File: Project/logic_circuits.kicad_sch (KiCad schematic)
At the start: 9 parts, among them SW1 Conn_01x02, U1 74LS04, U2 74LS93, U3 74LS08, U4 74LS32

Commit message: routing complete
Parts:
- removed unit 3 of U1
- removed unit 5 of U1
- removed unit 4 of U1
- added C8: 1uF, Capacitor_THT:CP_Radial_D5.0mm_P2.50mm, symbol Device:C
- added J1: Conn_01x04, Connector_PinHeader_2.54mm:PinHeader_1x04_P2.54mm_Vertical, symbol Connector_Generic:Conn_01x04
- added J2: Conn_02x07_Odd_Even, Connector_PinHeader_2.54mm:PinHeader_2x07_P2.54mm_Vertical, symbol Connector_Generic:Conn_02x07_Odd_Even
- added R3, R4, R5, R6, R7, R8, R9: 560, Resistor_THT:R_Axial_DIN0207_L6.3mm_D2.5mm_P7.62mm_Horizontal, symbol Device:R
- added unit 5 of U2
- added unit 3 of U2
- added unit 4 of U2
- renumbered C1 to C6, C2 to C7, U1 to U2, U2 to U5
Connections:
- net GND: now also U3.1, U3.2, C8.2, J1.4 (Pin_4), J2.10 (Pin_10), J2.12 (Pin_12), J2.14 (Pin_14), J2.2 (Pin_2), J2.4 (Pin_4), J2.6 (Pin_6), J2.8 (Pin_8); no longer U3.10, U3.9
- net Q0: now also U3.10, U2.9; no longer U3.1
- net Q1: now also U2.11
- net Q2: now also U3.9, U2.5; no longer U3.2
- net VCC: now also C8.1
- net a: now also R3.1, R8.1
- net b: now also U3.8, R4.1, R7.1; no longer U3.3
- net c: now also R5.1, R6.1
- net g: now also R9.1
- new net LED1: J2.1 (Pin_1), R3.2
- new net LED2: J2.3 (Pin_3), R4.2
- new net LED3: J2.5 (Pin_5), R5.2
- new net LED4: J2.7 (Pin_7), R6.2
- new net LED5: J2.9 (Pin_9), R7.2
- new net LED6: J2.11 (Pin_11), R8.2
- new net LED7: J2.13 (Pin_13), R9.2
- new net ~{Q0}: J1.1 (Pin_1), U2.8
- new net ~{Q1}: J1.2 (Pin_2), U2.10
- new net ~{Q2}: J1.3 (Pin_3), U2.6
- no-connect marks 7 -> 4
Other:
- note added: "Debug Output"
- note added: "Digital Dice Leds Layout"
- note added: "a"
- note added: "b"
- note added: "c"
- note added: "d"
- note added: "e"
- note added: "f"
- note added: "g"
- company: (none) -> Marcos Yonamine
- title: (none) -> Digital Dice
- moved on the sheet: C6, C7, R1, R2, SW1, U2A, U2B, U2F, U3B, U3D, U4A, U4B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

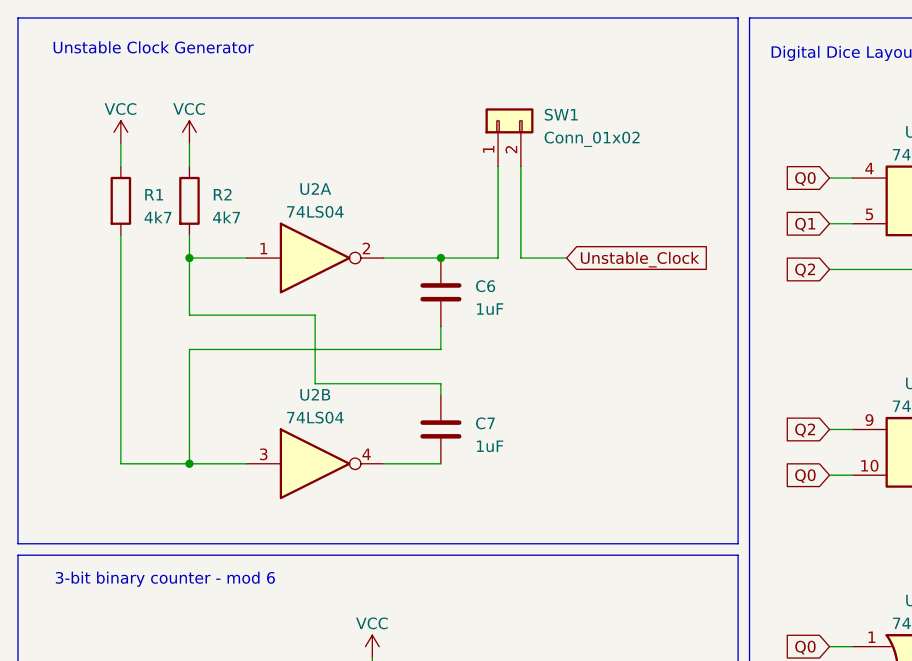
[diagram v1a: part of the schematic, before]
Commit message: fix #3
Latch was not unstable. Changed R1 and R2 to pulldown
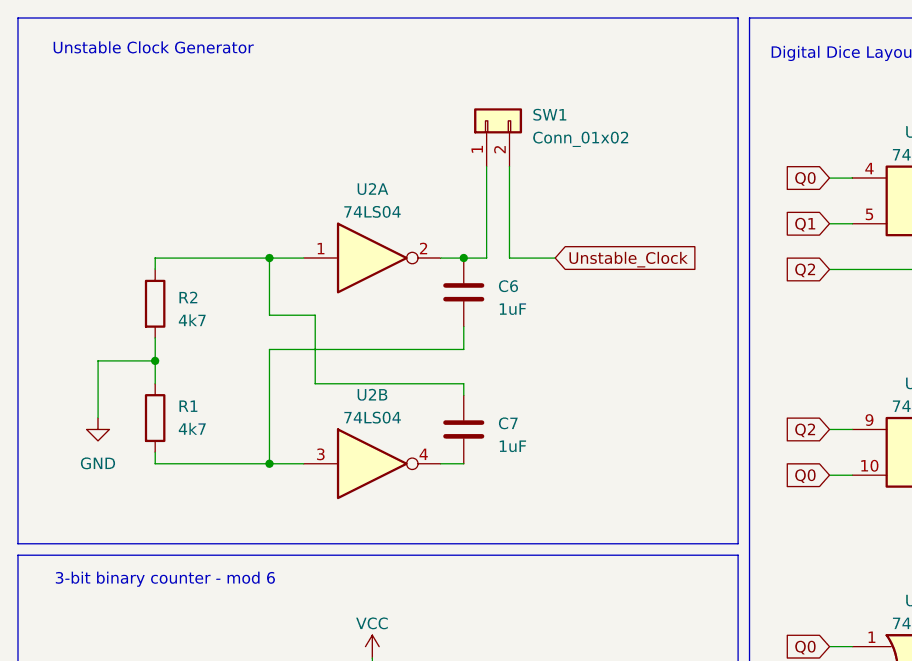
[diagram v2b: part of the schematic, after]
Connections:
- net GND: now also R1.1, R2.2
- net VCC: no longer R1.1, R2.1
- net at C7.1, U2.1: now also R2.1; no longer R2.2
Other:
- moved on the sheet: C6, C7, R2, SW1, U2A, U2B
